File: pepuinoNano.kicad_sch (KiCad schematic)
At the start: 33 parts, among them J1 USB_C_Receptacle_USB2.0_14P, J2 Conn_01x20, J3 Conn_01x20, J4 Conn_01x03, SW1 SW_Push, U1 RP2040, U3 W25Q16JVUXIQ TR, U4 MCP1700x-330xxTT, Y1 Crystal_GND24

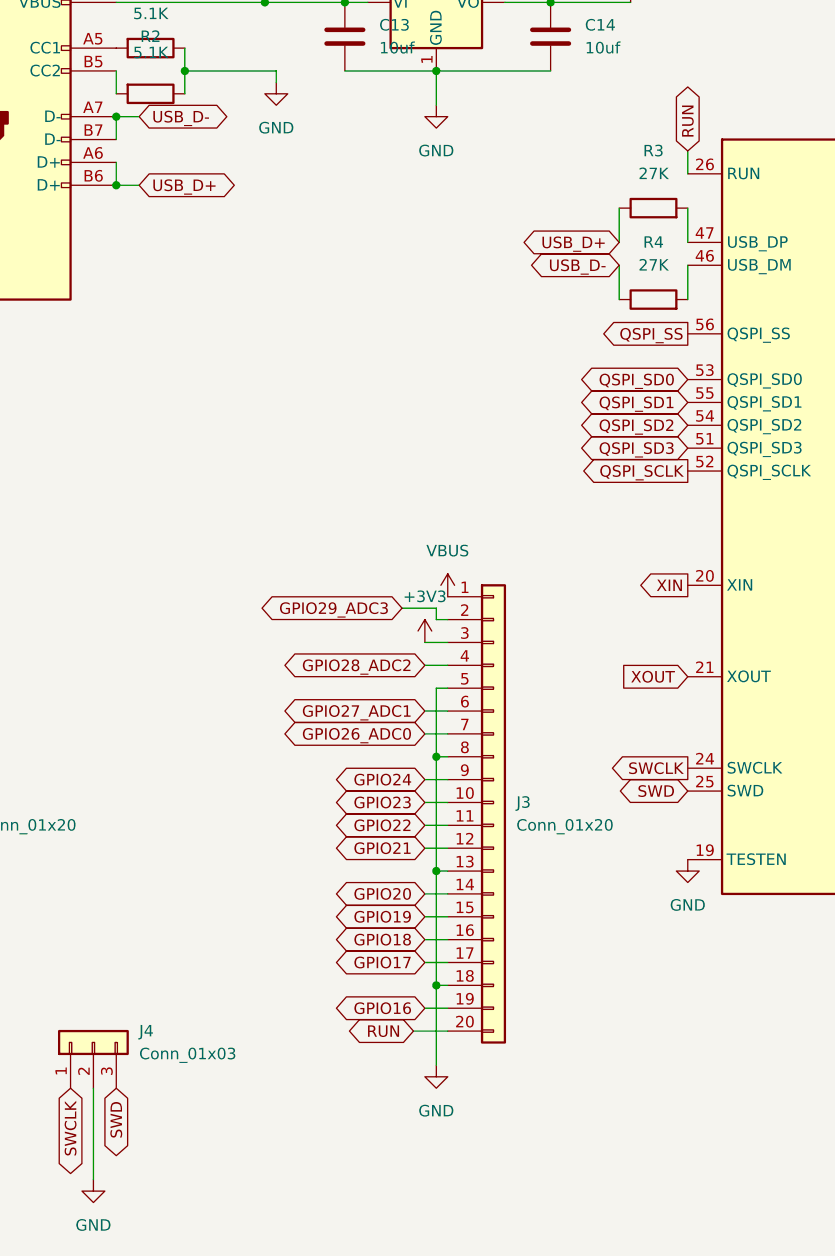
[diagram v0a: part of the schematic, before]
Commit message: update the resistor r3 and r4 from 27k to 27
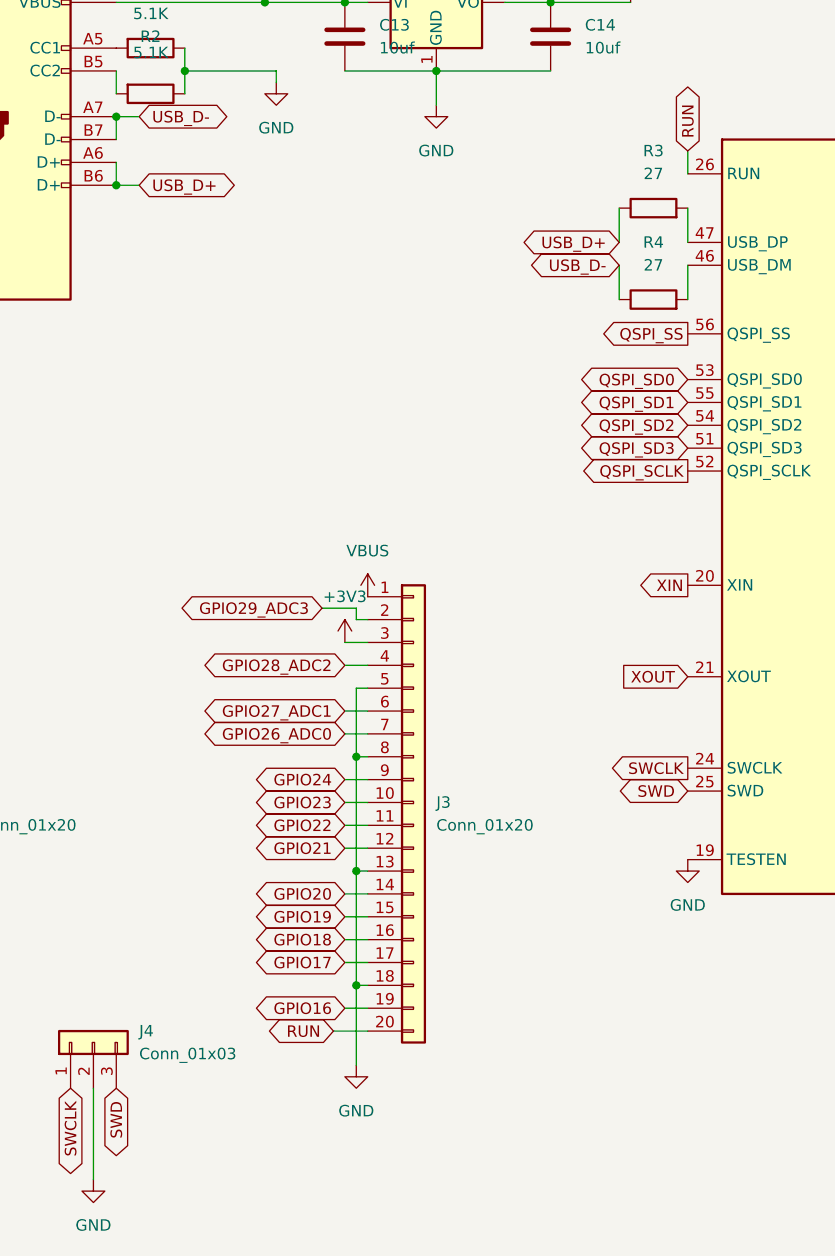
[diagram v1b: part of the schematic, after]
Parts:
- R3, R4: value 27K -> 27
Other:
- moved on the sheet: J3
